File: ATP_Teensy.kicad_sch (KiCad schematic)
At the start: 16 parts, among them J1 Screw_Terminal_01x02, U1 BMP388_3966, U2 L7805CV, U3 FT231X_XBee_USB_Adapter, U4 MPU6050, U5 Teensy4.1, U6 GPS

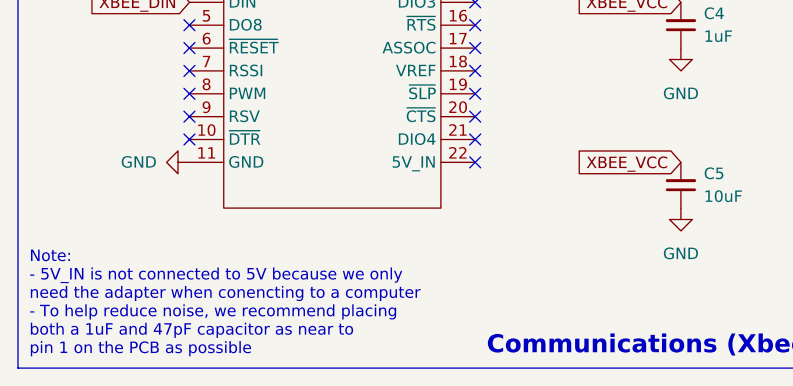
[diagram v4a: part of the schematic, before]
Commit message: Add notes to XBee adapter
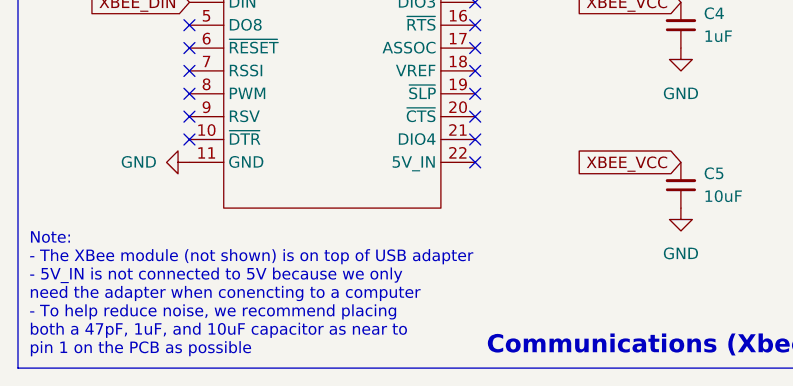
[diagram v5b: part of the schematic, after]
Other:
- note added: "Note: - The XBee module (not shown) is on top of USB adapter - 5V_IN is not connected to 5V because we only need the adapter when conencting to a computer - To help reduce noise, we recommend placing both a 47pF, 1uF, and 10uF capacitor as near to pin 1 on the PCB as possible"
- note removed: "Note: - 5V_IN is not connected to 5V because we only need the adapter when conencting to a computer - To help reduce noise, we recommend placing both a 1uF and 47pF capacitor as near to pin 1 on the PCB as possible"
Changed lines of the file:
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@@
     (effects (font (size 2 2) (thickness 0.4) bold) (justify left bottom))
   )
-  (text "Note:\n- 5V_IN is not connected to 5V because we only \nneed the adapter when conencting to a computer\n- To help reduce noise, we recommend placing \nboth a 1uF and 47pF capacitor as near to \npin 1 on the PCB as possible"
+  (text "Note:\n- The XBee module (not shown) is on top of USB adapter\n- 5V_IN is not connected to 5V because we only \nneed the adapter when conencting to a computer\n- To help reduce noise, we recommend placing \nboth a 47pF, 1uF, and 10uF capacitor as near to \npin 1 on the PCB as possible"
     (at 13.97 195.58 0)
     (effects (font (size 1.27 1.27)) (justify left bottom))

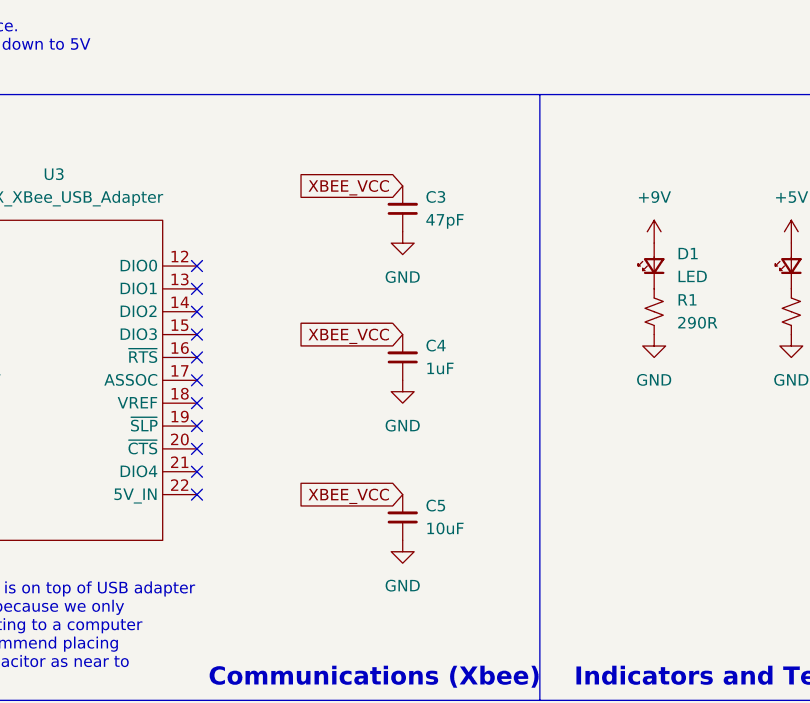
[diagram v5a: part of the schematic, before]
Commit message: Replace 10uF CER CAP with 10uF ELE CAP
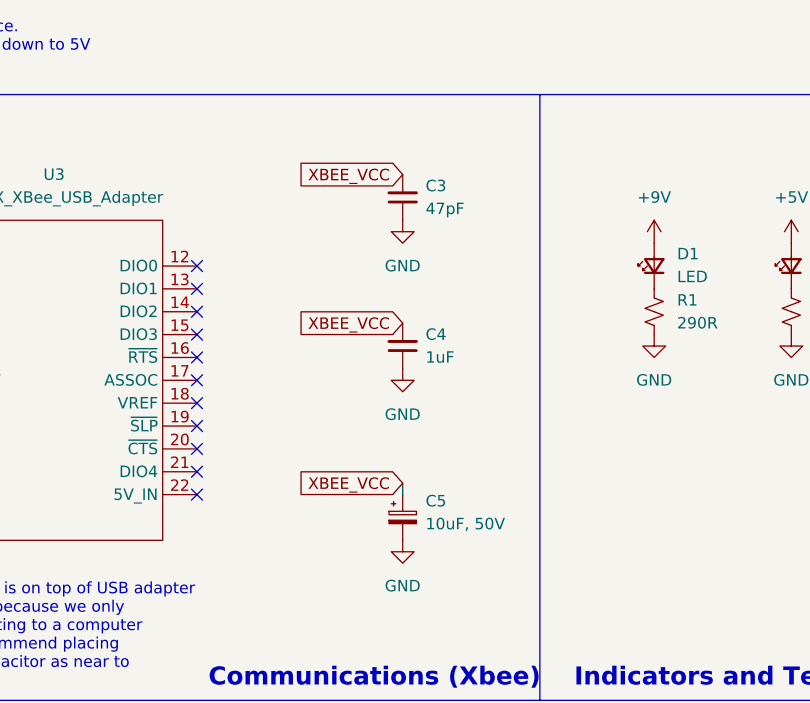
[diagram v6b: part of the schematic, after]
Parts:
- removed C5: 10uF, Capacitor_SMD:C_0805_2012Metric_Pad1.18x1.45mm_HandSolder, symbol Device:C_Small
- added C5: 10uF, 50V, Capacitor_SMD:CP_Elec_5x5.4, symbol Device:C_Polarized_Small
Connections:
- net GND: now also C5.2
- net XBEE_VCC: now also C5.1
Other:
- moved on the sheet: C3, C4

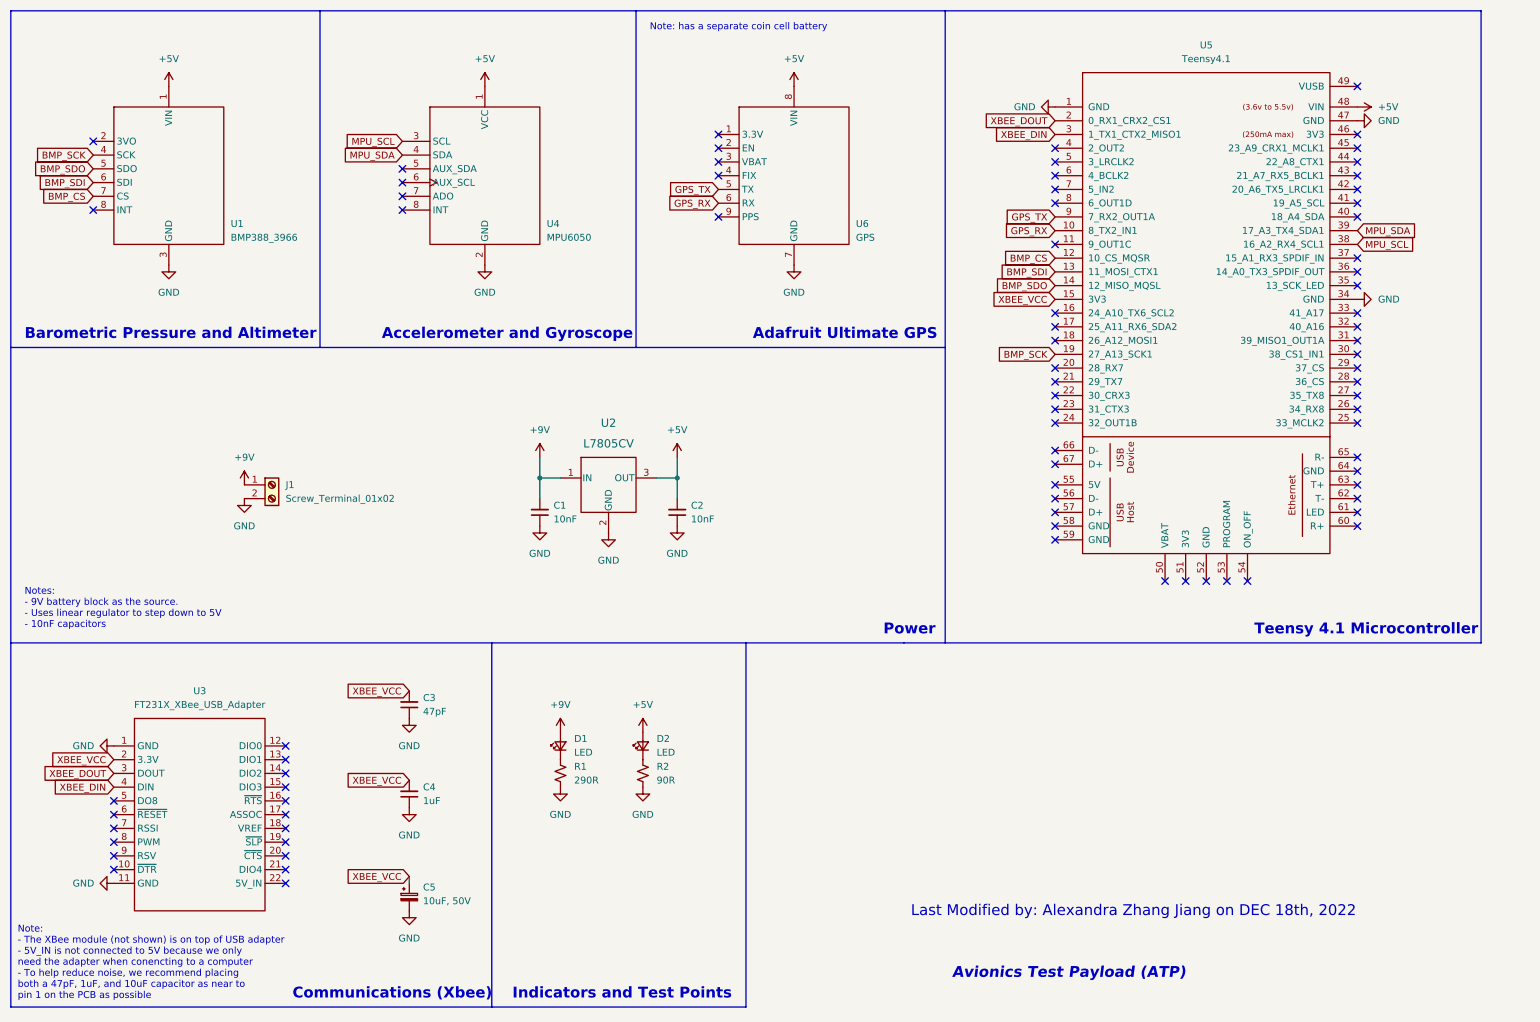
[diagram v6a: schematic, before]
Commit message: added spi and i2c connections, actual mounting holes, change xbee power input in the schematic
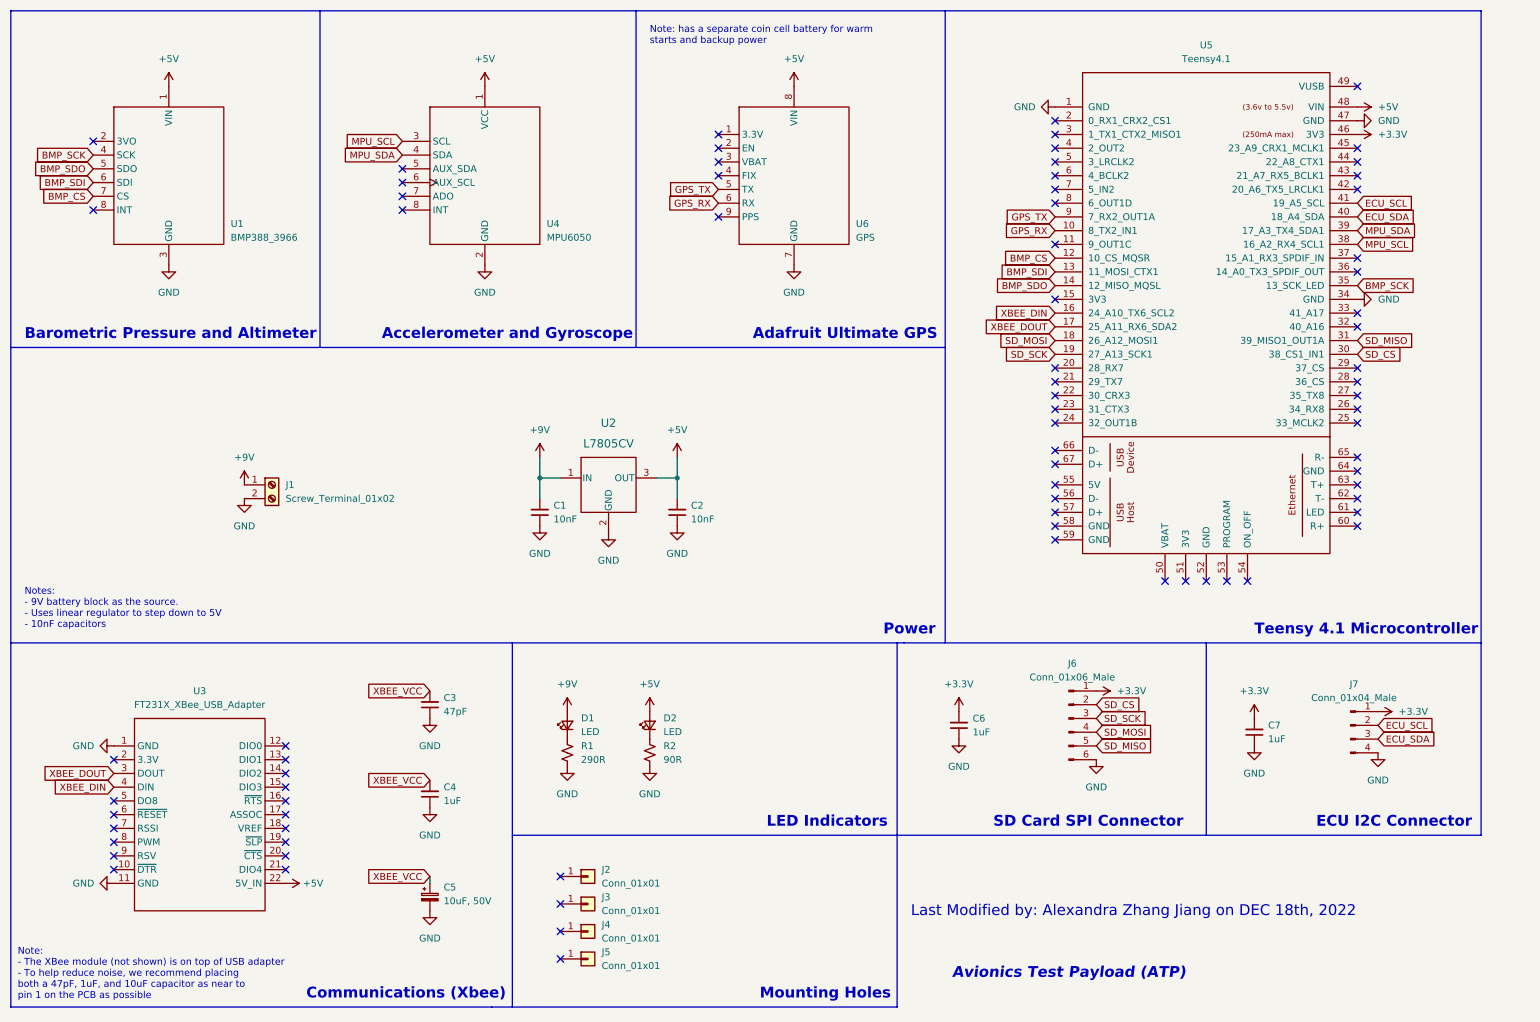
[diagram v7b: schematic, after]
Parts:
- added C6, C7: 1uF, Capacitor_SMD:C_0805_2012Metric_Pad1.18x1.45mm_HandSolder, symbol Device:C_Small
- added J2, J3, J4, J5: Conn_01x01, MountingHole:MountingHole_3.2mm_M3, symbol Connector_Generic:Conn_01x01
- added J6: Conn_01x06_Male, Connector_PinHeader_2.54mm:PinHeader_1x06_P2.54mm_Vertical, symbol Connector:Conn_01x06_Male
- added J7: Conn_01x04_Male, Connector_PinHeader_2.54mm:PinHeader_1x04_P2.54mm_Vertical, symbol Connector:Conn_01x04_Male
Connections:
- net +5V: now also U3.22 (5V_IN)
- net BMP_SCK: now also U5.35 (13_SCK_LED); no longer U5.19 (27_A13_SCK1)
- net GND: now also C6.1, C7.1, J6.6 (Pin_6), J7.4 (Pin_4)
- net XBEE_DIN: now also U5.16 (24_A10_TX6_SCL2); no longer U5.3 (1_TX1_CTX2_MISO1)
- net XBEE_DOUT: now also U5.17 (25_A11_RX6_SDA2); no longer U5.2 (0_RX1_CRX2_CS1)
- net XBEE_VCC: no longer U3.2 (3.3V), U5.15 (3V3)
- net SD_MOSI: now reaches U5.18 (26_A12_MOSI1)
- net SD_MOSI: now also J6.4 (Pin_4)
- net SD_CS: now reaches U5.30 (38_CS1_IN1)
- net SD_CS: now also J6.2 (Pin_2)
- net SD_MISO: now reaches U5.31 (39_MISO1_OUT1A)
- net SD_MISO: now also J6.5 (Pin_5)
- net ECU_SDA: now reaches U5.40 (18_A4_SDA)
- net ECU_SDA: now also J7.3 (Pin_3)
- net ECU_SCL: now reaches U5.41 (19_A5_SCL)
- net ECU_SCL: now also J7.2 (Pin_2)
- net +3.3V: now reaches U5.46 (3V3)
- net +3.3V: now also C6.2, C7.2, J6.1 (Pin_1), J7.1 (Pin_1)
- new net SD_SCK: J6.3 (Pin_3), U5.19 (27_A13_SCK1)
- no-connect marks 80 -> 78
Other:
- note added: "ECU I2C Connector"
- note added: "LED Indicators"
- note added: "Mounting Holes"
- note added: "Note: - The XBee module (not shown) is on top of USB adapter - To help reduce noise, we recommend placing both a 47pF, 1uF, and 10uF capacitor as near to pin 1 on the PCB as possible"
- note added: "Note: has a separate coin cell battery for warm starts and backup power"
- note added: "SD Card SPI Connector"
- note removed: "Indicators and Test Points"
- note removed: "Note: - The XBee module (not shown) is on top of USB adapter - 5V_IN is not connected to 5V because we only need the adapter when conencting to a computer - To help reduce noise, we recommend placing both a 47pF, 1uF, and 10uF capacitor as near to pin 1 on the PCB as possible"
- note removed: "Note: has a separate coin cell battery"
- moved on the sheet: C3, C4, C5, D1, D2, R1, R2

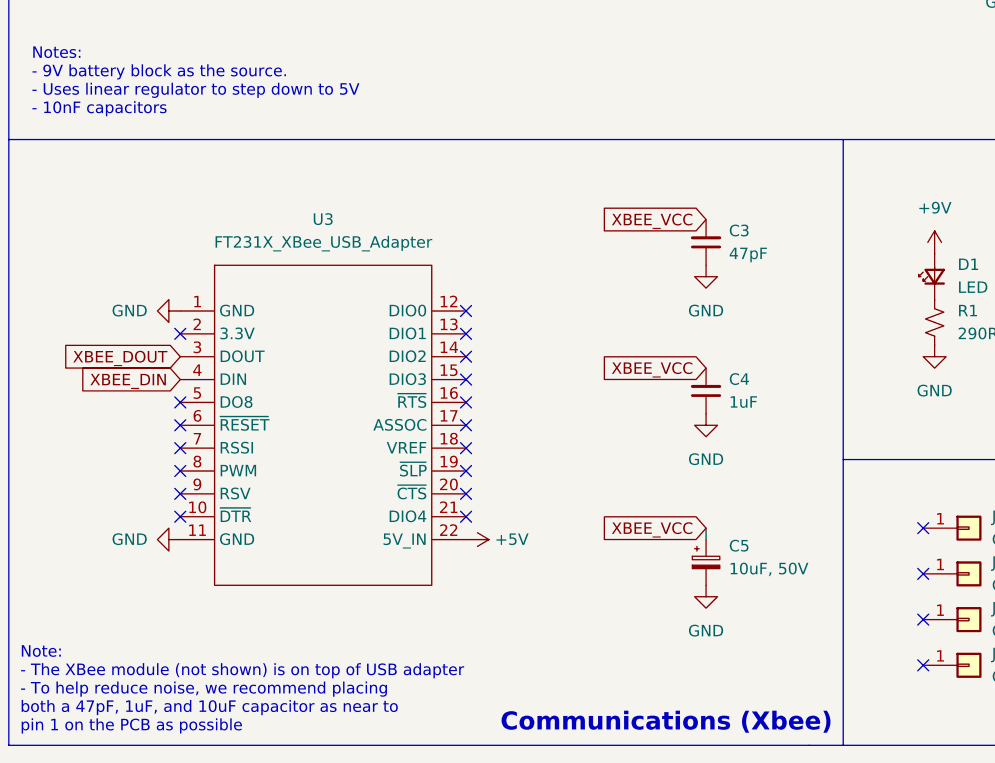
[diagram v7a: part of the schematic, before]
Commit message: v1.1 Layout done, change direction of reg, added spi and i2c extensions
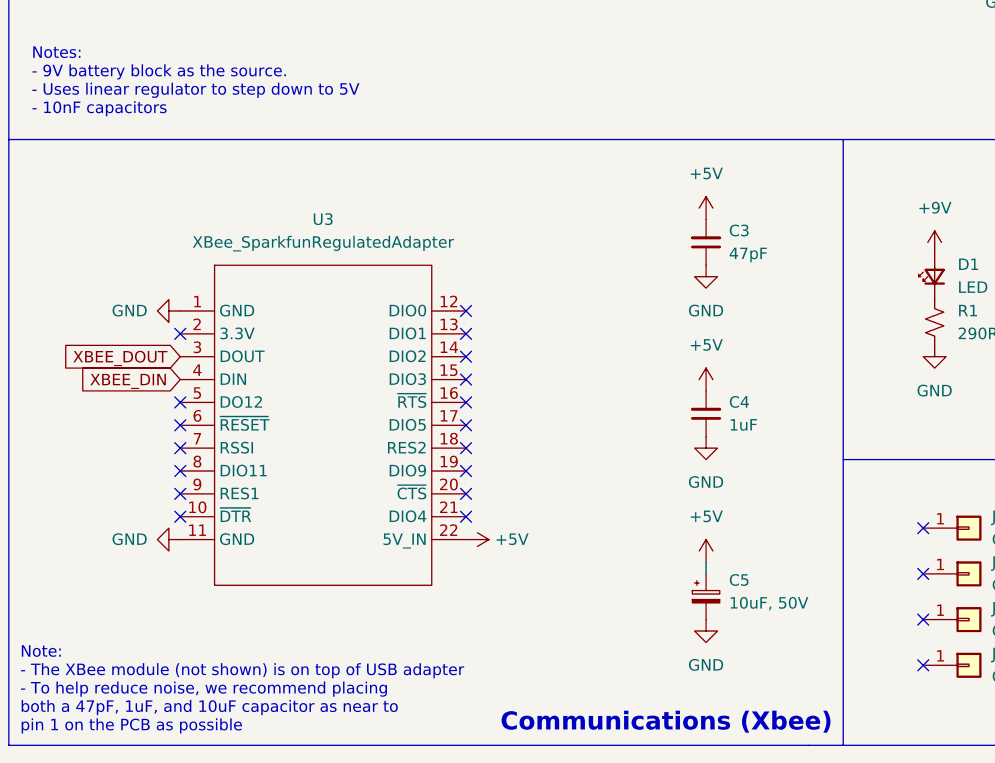
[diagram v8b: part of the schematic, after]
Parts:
- removed U3: FT231X_XBee_USB_Adapter, ATP_Teensy_footprints:XBee_Adapter, symbol ATP_Teensy-lib:FT231X_XBee_USB_Adapter
- added U3: XBee_SparkfunRegulatedAdapter, ATP_Teensy_footprints:XBee_SparkfunAdapter, symbol ATP_Teensy-lib:XBee_SparkfunRegulatedAdapter
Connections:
- net XBEE_VCC is gone; now on net +5V: C3.2, C4.2, C5.1
- net +5V: now also U3.22 (5V_IN)
- net GND: now also U3.1 (GND), U3.11 (GND)
- net XBEE_DIN: now also U3.4 (DIN)
- net XBEE_DOUT: now also U3.3 (DOUT)
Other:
- moved on the sheet: C4, C5
